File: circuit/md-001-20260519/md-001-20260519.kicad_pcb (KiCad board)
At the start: 2 copper layers, 71.4 x 17.3 mm, 38 parts, among them J1 VIN-motor, J2 Conn-relay

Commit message: Update いろいろ
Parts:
- moved J1 5.33 mm to (14.0, -51.5)
- moved J2 2.02 mm to (-15.7, -50.1)
- moved C10 1.10 mm to (-62.4, -50.7)
- moved C3 1.10 mm to (-66.4, -53.2)
- moved C4 1.10 mm to (-66.4, -50.7)
- moved C9 1.10 mm to (-62.4, -53.2)
- moved R1 1.10 mm to (-58.4, -53.2)
- moved R13 1.10 mm to (-50.4, -53.2)
- moved R14 1.10 mm to (-50.4, -50.7)
- moved R2 1.10 mm to (-58.4, -50.7)
- moved R7 1.10 mm to (-54.4, -53.2)
- moved R8 1.10 mm to (-54.4, -50.7)
- moved U1 1.10 mm to (-24.4, -54.8)
- moved U2 1.10 mm to (-16.5, -57.7)
- moved U3 1.10 mm to (-8.35, -59.4)
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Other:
- board size 71.4 x 17.3 mm -> 71.4 x 21.3 mm

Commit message: Update ちょっとだけ進めてみたけど...
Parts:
- C1, C15, C16, C3, R1, R3, R4, R7: moved to B.Cu
- moved C15 58.9 mm to (11.8, -44.7), turned to 180 degrees
- moved C16 57.9 mm to (11.8, -47.2), turned to 180 degrees
- moved C3 44.4 mm to (-22.1, -54.1), turned to -65 degrees
- moved C1 43.0 mm to (-23.4, -57.1), turned to -65 degrees
- moved R4 31.7 mm to (-27.3, -51.7), turned to -65 degrees
- moved R1 29.8 mm to (-28.6, -54.6), turned to -65 degrees
- moved R3 28.5 mm to (-30.5, -53.8), turned to 115 degrees
- moved R7 25.4 mm to (-29.1, -50.9), turned to -65 degrees
- moved U4 8.80 mm to (8.75, -59.0), turned to -8 degrees
- moved U3 5.61 mm to (-2.74, -59.5), turned to 3 degrees
- moved U2 2.43 mm to (-14.1, -57.8), turned to 14 degrees
- moved U1 1.05 mm to (-25.4, -54.4), turned to 25 degrees
- moved C10 0.55 mm to (-62.0, -50.3)
- moved C11 0.55 mm to (-62.0, -47.8)
- moved C12 0.55 mm to (-62.0, -45.3)
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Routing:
- net VREF-1: track 0.00 -> 4.47 mm, vias 0 -> 1
- net Net-(U1-CPL): track 0.00 -> 3.34 mm, vias 0 -> 1
- net IMODE-1: track 0.00 -> 3.15 mm, vias 0 -> 1
- net Net-(U1-CPH): track 0.00 -> 2.92 mm, vias 0 -> 1
- net Net-(U1-VCP): track 0.00 -> 2.92 mm, vias 0 -> 1
- net Net-(U1-IPROPI): track 0.00 -> 2.07 mm, vias 0 -> 1
- added copper zone on B.Cu, net GND
- added copper zone on F.Cu, net GND
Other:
- outline, holes or cut-outs redrawn
- board text added: "MD-01"

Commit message: Update MD基板に触れた
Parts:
- C2, C4, R2, R5, R6, R8: moved to B.Cu
- moved C4 55.1 mm to (-11.3, -57.3), turned to -76 degrees
- moved C2 54.2 mm to (-12.1, -60.5), turned to -76 degrees
- moved R2 41.3 mm to (-17.7, -59.1), turned to -76 degrees
- moved R6 37.1 mm to (-16.9, -55.9), turned to -76 degrees
- moved R8 35.5 mm to (-18.8, -55.5), turned to -76 degrees
- moved R5 34.4 mm to (-19.6, -58.6), turned to 104 degrees
- moved C10 0.55 mm to (-62.4, -50.7)
- moved C11 0.55 mm to (-62.4, -48.2)
- moved C12 0.55 mm to (-62.4, -45.7)
- moved C7 0.55 mm to (-62.4, -58.2)
- moved C8 0.55 mm to (-62.4, -55.7)
- moved C9 0.55 mm to (-62.4, -53.2)
- moved C15 0.55 mm to (11.4, -45.1)
- moved C16 0.55 mm to (11.4, -47.6)
- moved J1 0.55 mm to (14.0, -51.5)
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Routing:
- net VREF-2: track 0.00 -> 4.47 mm, vias 0 -> 1
- net Net-(U2-CPL): track 0.00 -> 3.34 mm, vias 0 -> 1
- net IMODE-2: track 0.00 -> 3.15 mm, vias 0 -> 1
- net Net-(U2-VCP): track 0.00 -> 2.92 mm, vias 0 -> 1
- net Net-(U2-CPH): track 0.00 -> 2.92 mm, vias 0 -> 1
- net Net-(U2-IPROPI): track 0.00 -> 2.07 mm, vias 0 -> 1

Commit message: Update いったんMD完成
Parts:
- removed C15, C16: 100μ, Resistor_SMD:R_1206_3216Metric
- C10, C11, C12, C13, C5, C6, C7, C8, C9, R10, R11, R12, R13, R14, R15, R16, R9: moved to B.Cu
- C14: value 100n -> 100μ; footprint Resistor_SMD:R_0603_1608Metric -> Resistor_SMD:R_1206_3216Metric; moved to B.Cu
- moved C6 79.3 mm to (11.4, -60.6), turned to -98 degrees
- moved C8 73.4 mm to (11.0, -57.4), turned to -98 degrees
- moved C12 72.1 mm to (8.36, -59.4), turned to -98 degrees
- moved C13 70.7 mm to (11.5, -48.0), turned to 180 degrees
- moved C14 70.7 mm to (11.5, -45.5), turned to 180 degrees
- moved C5 67.4 mm to (-0.37, -61.7), turned to -87 degrees
- moved C7 62.2 mm to (-0.20, -58.4), turned to -87 degrees
- moved R10 62.2 mm to (5.76, -61.4), turned to -98 degrees
- moved C11 60.4 mm to (-3.14, -59.9), turned to -87 degrees
- moved R14 56.2 mm to (5.30, -58.2), turned to -98 degrees
- moved R16 55.2 mm to (3.32, -58.5), turned to -98 degrees
- moved R13 54.8 mm to (3.78, -61.7), turned to 82 degrees
- moved R9 50.1 mm to (-6.08, -61.4), turned to -87 degrees
- moved C10 48.5 mm to (-14.5, -58.2), turned to -76 degrees
- moved R12 44.6 mm to (-5.91, -58.1), turned to -87 degrees
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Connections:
- J2 pad 1: +3.3V -> OUT2-1
- J2 pad 10: OUT2-2 -> PH-2
- J2 pad 11: OUT1-3 -> OUT1-4
- J2 pad 12: OUT2-3 -> PH-3
- J2 pad 13: OUT1-4 -> OUT2-4
- J2 pad 14: OUT2-4 -> PH-4
- J2 pad 2: EN -> OUT1-1
- J2 pad 3: PH-1 -> OUT1-2
- J2 pad 4: PH-2 -> +3.3V
- J2 pad 5: PH-3 -> OUT2-2
- J2 pad 6: PH-4 -> EN
- J2 pad 7: OUT1-1 -> OUT1-3
- J2 pad 8: OUT2-1 -> PH-1
- J2 pad 9: OUT1-2 -> OUT2-3
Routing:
- net EN: track 0.00 -> 73.5 mm
- net GND: track 0.00 -> 45.0 mm, vias 0 -> 4
- net +3.3V: track 0.00 -> 38.2 mm, vias 0 -> 4
- net PH-1: track 0.00 -> 32.2 mm, vias 0 -> 1
- net PH-2: track 0.00 -> 26.7 mm, vias 0 -> 1
- net VCC: track 0.00 -> 22.2 mm, vias 0 -> 4
- net PH-3: track 0.00 -> 20.2 mm, vias 0 -> 1
- net PH-4: track 0.00 -> 19.8 mm, vias 0 -> 1
- net OUT2-4: track 0.00 -> 17.5 mm, vias 0 -> 1
- net OUT1-1: track 0.00 -> 13.2 mm, vias 0 -> 1
- net OUT2-3: track 0.00 -> 12.4 mm, vias 0 -> 1
- net OUT1-4: track 0.00 -> 12.2 mm, vias 0 -> 1
- net OUT2-2: track 0.00 -> 9.15 mm, vias 0 -> 1
- net OUT1-3: track 0.00 -> 8.31 mm, vias 0 -> 1
- net OUT2-1: track 0.00 -> 8.21 mm, vias 0 -> 1
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- added copper zone on In1.Cu, net +3.3V
- added copper zone on F.Cu, net VCC
- removed copper zone on F.Cu, net GND
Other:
- outline, holes or cut-outs redrawn
- copper layers 2 -> 4
- board text added: "MD01"
- board text removed: "MD-01"

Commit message: Update DRしてもらったのでMDを修正更新
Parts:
- turned C13 to 0 degrees
- turned C14 to 0 degrees
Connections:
- J1 pad 1: VCC -> GND
- J1 pad 2: GND -> VCC

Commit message: Update MD基板を更新
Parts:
- added J3: Conn_relay, Connector_PinSocket_2.54mm:PinSocket_2x08_P2.54mm_Horizontal, F.Cu at (-18.2, -50.1)
- J2: value Conn-relay -> Conn_Ball_Catch; footprint Connector_PinSocket_2.54mm:PinSocket_2x07_P2.54mm_Horizontal -> Connector_PinSocket_2.54mm:PinSocket_1x03_P2.54mm_Vertical
- moved J2 40.7 mm to (25.0, -50.0), turned to 180 degrees
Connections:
- J2 pad 1: OUT2-1 -> BALL_CATCH
- J2 pad 2: OUT1-1 -> +3.3V
- J2 pad 3: OUT1-2 -> GND
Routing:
- net BALL_CATCH: track 0.00 -> 26.4 mm
- net PH-4: track 19.8 -> 25.0 mm
- net OUT1-1: track 13.2 -> 10.3 mm
- net PH-1: track 32.2 -> 29.7 mm
- net EN: track 73.5 -> 71.0 mm
- net PH-2: track 26.7 -> 24.2 mm
- net PH-3: track 20.2 -> 19.2 mm
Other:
- outline, holes or cut-outs redrawn

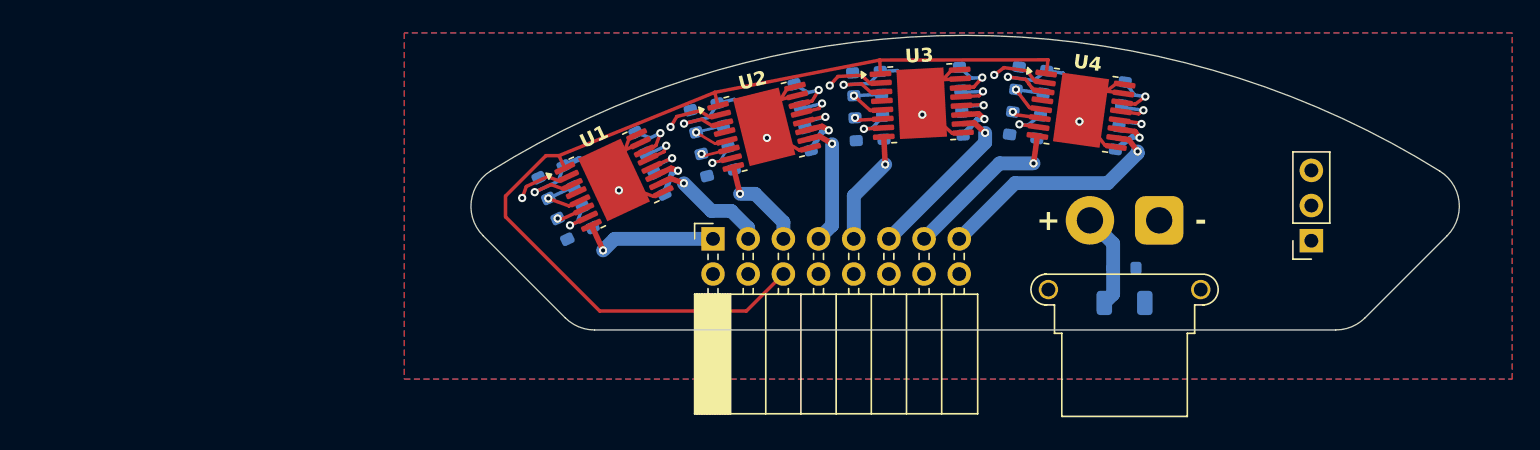
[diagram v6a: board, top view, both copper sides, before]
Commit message: Update MD基板のボード図を更新
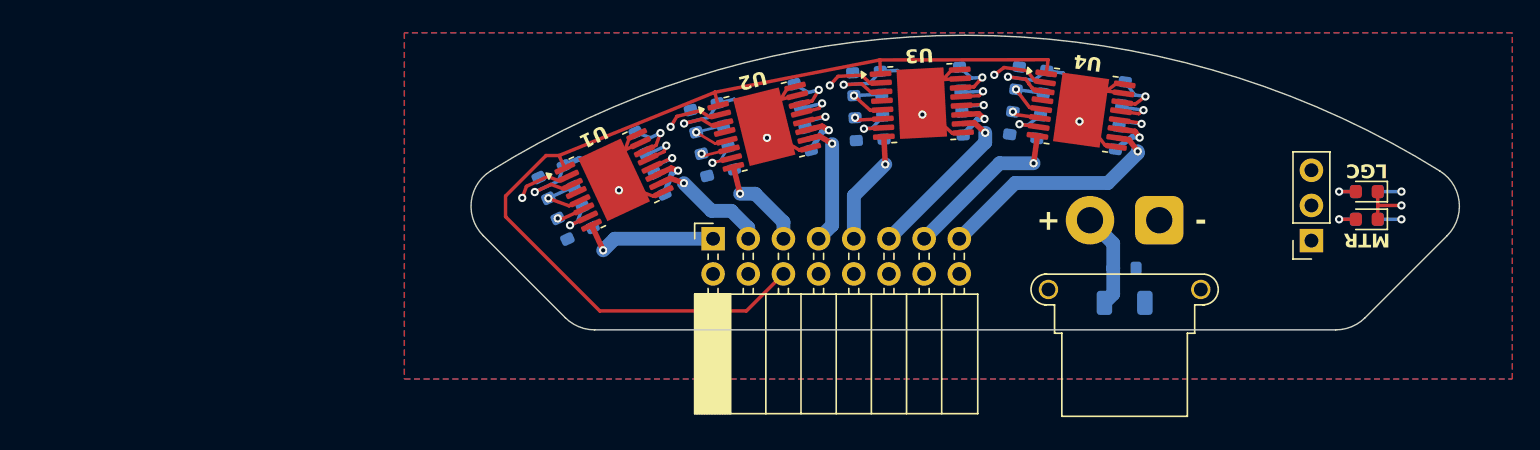
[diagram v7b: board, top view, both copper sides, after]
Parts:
- added D1: MTR_PWR, LED_SMD:LED_0603_1608Metric, F.Cu at (29.0, -51.5)
- added D2: LGC_PWR, LED_SMD:LED_0603_1608Metric, F.Cu at (29.0, -53.5)
- added R17: 2.49k, Resistor_SMD:R_0603_1608Metric, B.Cu at (29.0, -51.5)
- added R18: 330, Resistor_SMD:R_0603_1608Metric, B.Cu at (29.0, -53.5)
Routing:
- net GND: track 45.0 -> 48.8 mm, vias 4 -> 5
- net Net-(D2-A): track 0.00 -> 2.39 mm, vias 0 -> 1
- net Net-(D1-A): track 0.00 -> 2.39 mm, vias 0 -> 1
- net VCC: track 22.2 -> 23.9 mm, vias 4 -> 5
- net +3.3V: track 38.2 -> 39.9 mm, vias 4 -> 5
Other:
- board text added: "LGC"
- board text added: "MTR"

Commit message: Create メイン基板、MD基板、キッカー基板の発注ファイルを作成
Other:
- board text added: "MD-001"
- board text removed: "MD01"
